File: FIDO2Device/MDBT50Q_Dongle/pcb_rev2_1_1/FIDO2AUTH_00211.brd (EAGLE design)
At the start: 19.7 x 35.6 mm, 39 parts, among them CN1 TE-1734028, CN2 IF_4PIN, CN5 IF_2PIN_SOL, SW1 SKRPACE010, SW2 SKTADAE010, U1 MDBT50Q-P1M, U2 XC6206P332MR-G, U3 ATECC608A-MAHDA-S, X1 NX3215SA-32.768K

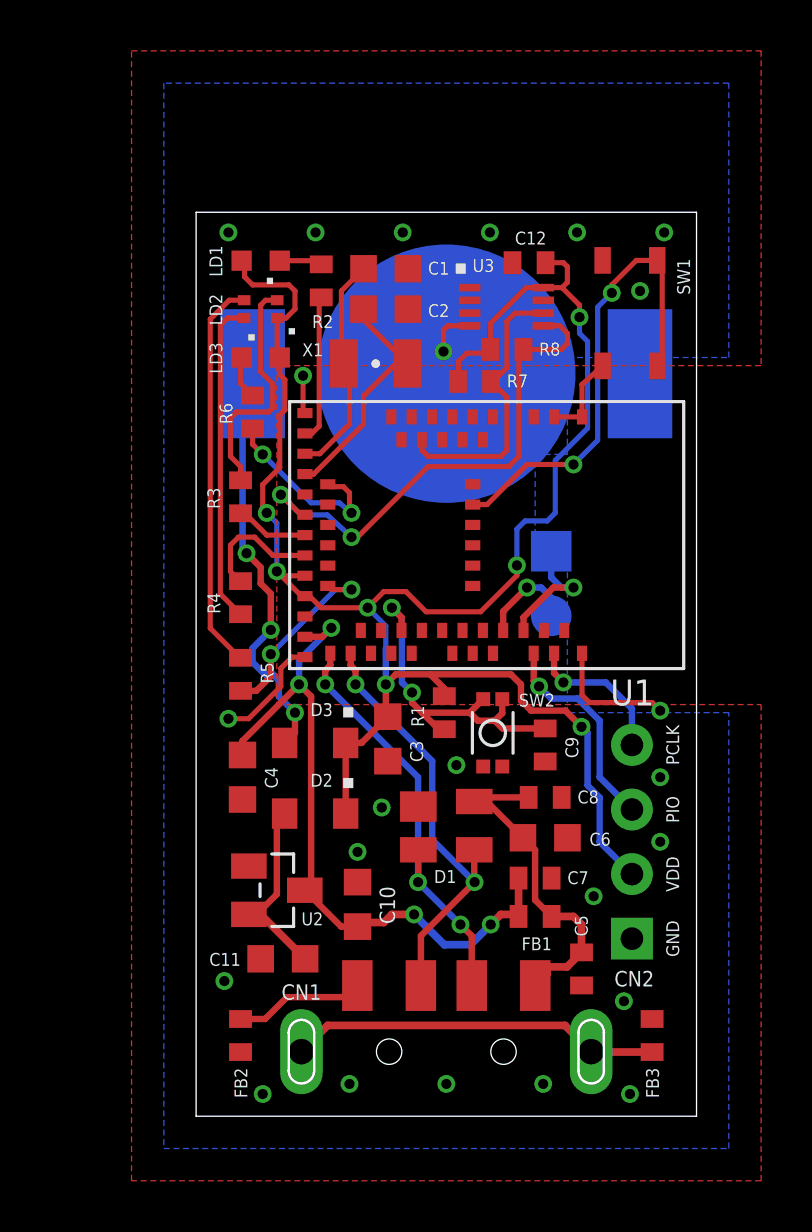
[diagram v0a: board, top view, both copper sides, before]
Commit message: プリント基板設計データを修正
・チップコンデンサー／フェライトビーズのパッドパターン間隔を拡張
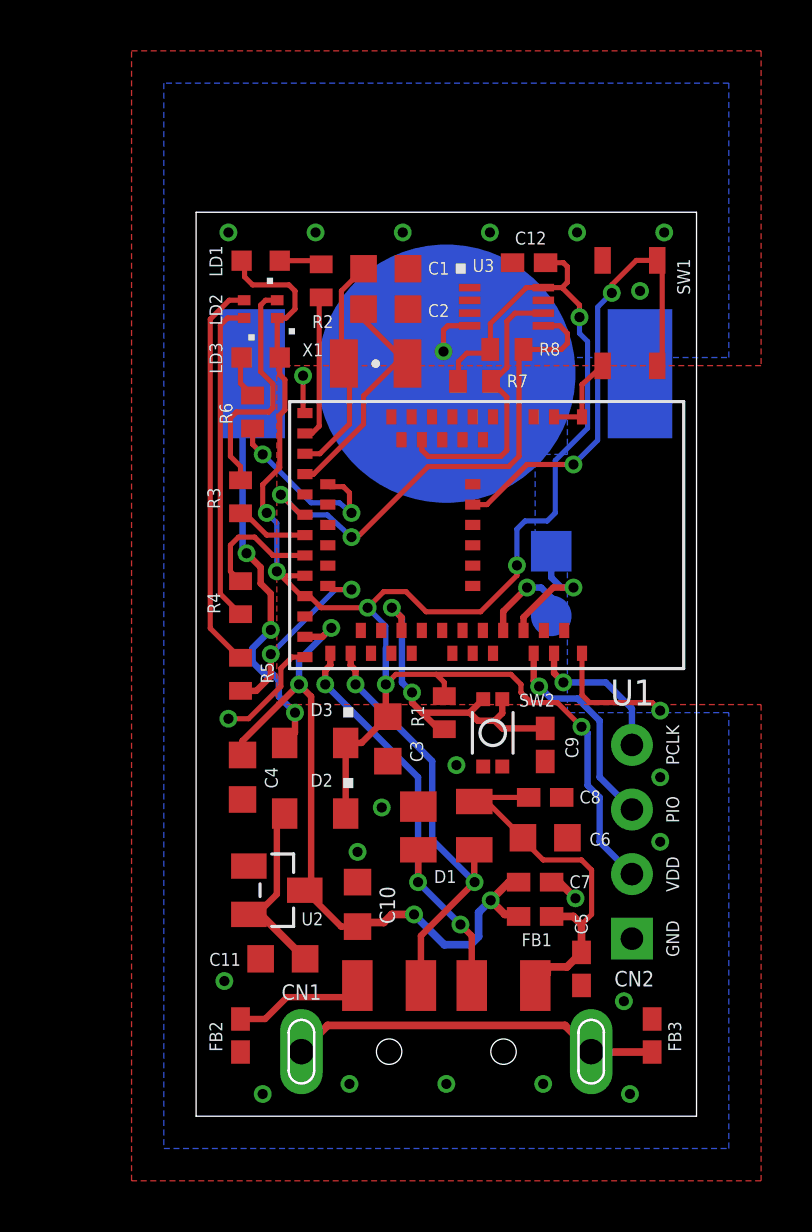
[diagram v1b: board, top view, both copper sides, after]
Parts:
- C12, C5, C7, C8, C9, FB1, FB2, FB3: device Parts:C0402 -> Parts:C0402K
- moved C7 0.16 mm to (16.5, 9.21)
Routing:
- net VBUS: track 13.2 -> 15.2 mm
- net 0V: track 16.4 -> 17.6 mm
- net VBUS_NRF: track 28.1 -> 29.0 mm

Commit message: 部品レイアウトの見直し
・回路図変更は無し
・電源系配線の見直し
・差動信号配線の見直し（ベンディングを少なくする）
・GNDパターンの見直し
・１点未配線あり
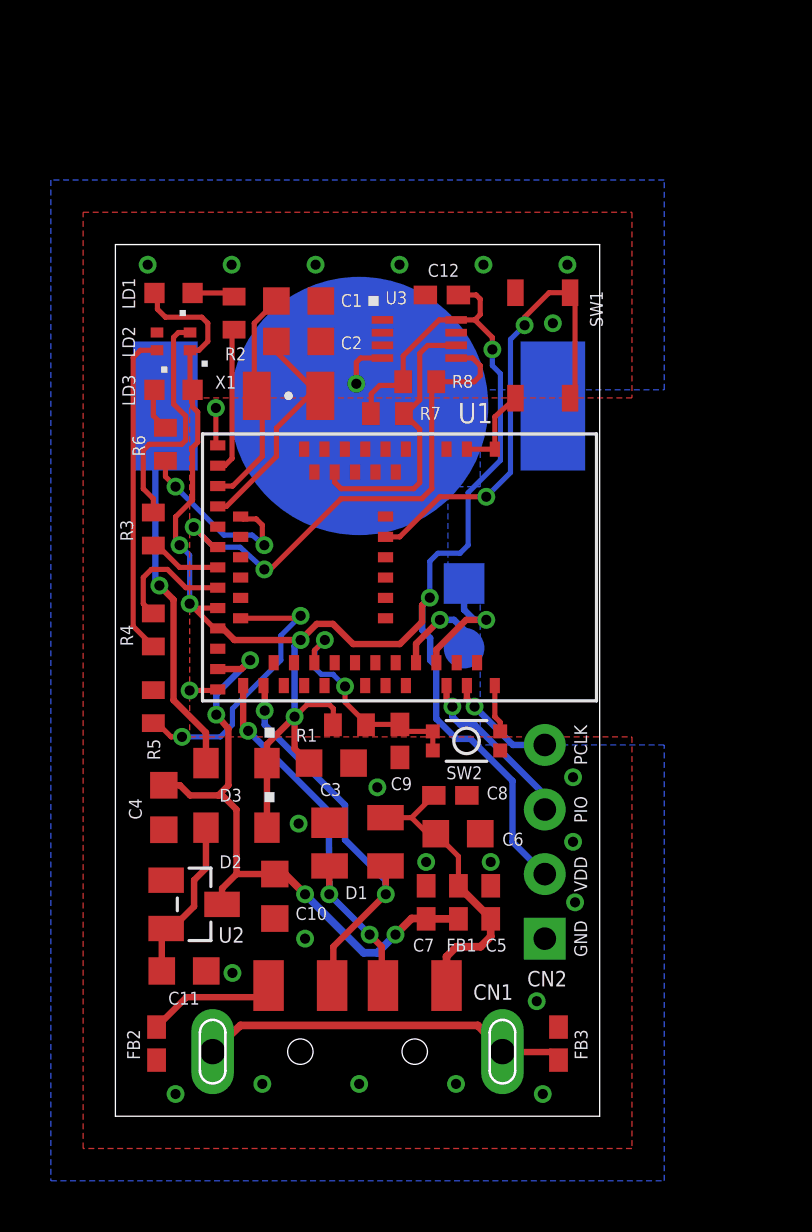
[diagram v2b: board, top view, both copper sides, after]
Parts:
- moved C9 5.72 mm to (11.2, 14.8)
- moved C5 4.43 mm to (14.8, 8.41), turned to 90 degrees
- moved C7 4.36 mm to (12.2, 8.41), turned to 90 degrees
- moved C11 3.92 mm to (2.70, 5.71), turned to 0 degrees
- moved R1 3.76 mm to (9.21, 15.4), turned to 0 degrees
- moved C8 3.73 mm to (13.2, 12.6)
- moved FB3 3.70 mm to (17.4, 2.86)
- moved C12 3.66 mm to (12.8, 32.3)
- moved SW1 3.66 mm to (16.8, 30.3)
- moved CN5 3.66 mm to (13.7, 21.0)
- moved R8 3.66 mm to (12.0, 28.9)
- moved LD1 3.66 mm to (2.29, 32.4)
- moved X1 3.66 mm to (6.81, 28.3)
- moved BAT1 3.66 mm to (9.59, 27.9)
- moved C2 3.66 mm to (7.21, 30.5)
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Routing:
- net N$7: track 15.5 -> 0.03 mm
- net 0V: track 17.6 -> 9.97 mm, vias 24 -> 25
- net RESET: track 13.7 -> 9.20 mm
- net LED2_B: track 7.54 -> 11.4 mm
- net VBUS: track 15.2 -> 11.6 mm
- net VBUS_NRF: track 29.0 -> 25.5 mm
- net D_N: track 16.8 -> 15.2 mm
- net SWDIO: track 8.35 -> 6.80 mm
- net SWDCLK: track 5.85 -> 4.34 mm
- net D_P: track 17.2 -> 15.8 mm
- net N$5: track 16.5 -> 15.0 mm, vias 3 -> 1
- net N$4: track 7.29 -> 6.49 mm
- net VDD_NRF: track 75.6 -> 75.5 mm, vias 7 -> 6
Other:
- board size 19.7 x 35.6 mm -> 19.1 x 34.3 mm

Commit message: 部品レイアウトの見直し
・未配線を解決
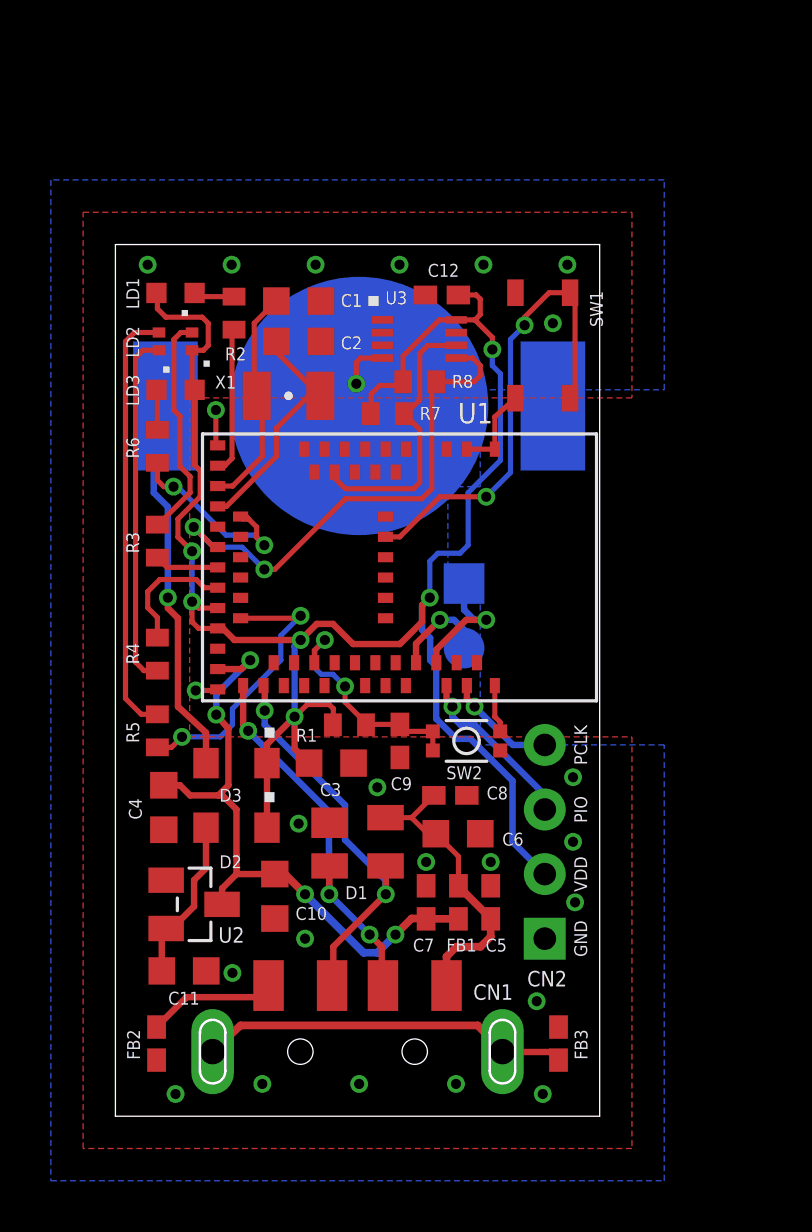
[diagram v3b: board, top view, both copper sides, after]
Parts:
- moved R4 0.97 mm to (1.65, 18.2)
- moved R5 0.97 mm to (1.65, 15.2)
- moved R3 0.50 mm to (1.65, 22.6)
- moved R6 0.33 mm to (1.65, 26.4)
- moved LD1 0.08 mm to (2.37, 32.4)
- moved LD2 0.08 mm to (2.37, 30.5)
- moved LD3 0.08 mm to (2.37, 28.6)
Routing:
- net N$7: track 0.03 -> 17.0 mm
- net N$6: track 12.7 -> 14.0 mm
- net LED3: track 7.47 -> 8.11 mm
- net N$5: track 15.0 -> 15.5 mm

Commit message: 部品レイアウトの見直し
・GNDビアの位置を調整
・R4、R5の向きを変えて配線を改善
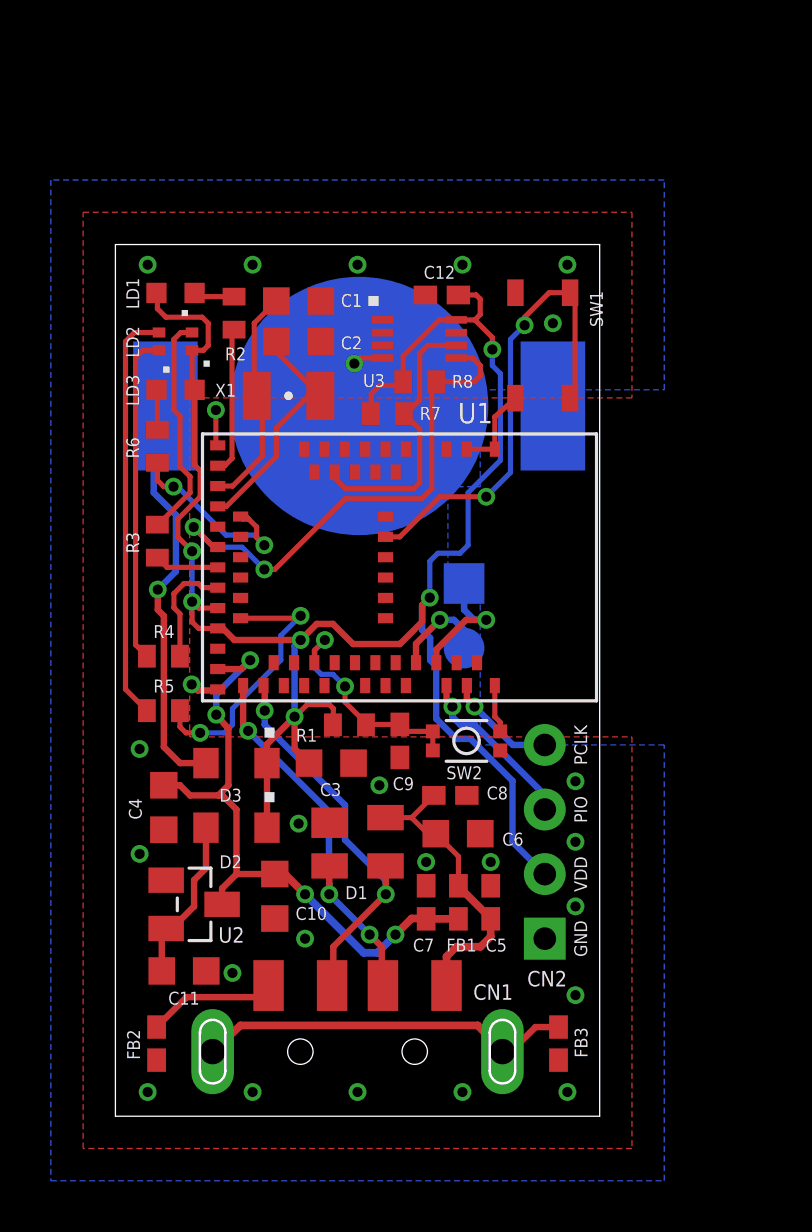
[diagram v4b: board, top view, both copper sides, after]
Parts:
- moved R5 0.83 mm to (1.89, 16.0), turned to 180 degrees
- moved R4 0.25 mm to (1.89, 18.1), turned to 180 degrees
- turned FB3 to 270 degrees
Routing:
- net N$5: track 15.5 -> 16.7 mm
- net N$6: track 14.0 -> 13.0 mm
- net N$7: track 17.0 -> 16.3 mm
- net LED2_G: track 5.06 -> 4.52 mm
- net 0V: track 9.66 -> 9.17 mm, vias 25 -> 26
